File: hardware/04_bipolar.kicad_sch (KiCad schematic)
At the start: 22 parts, among them U4 TPS65131RGER

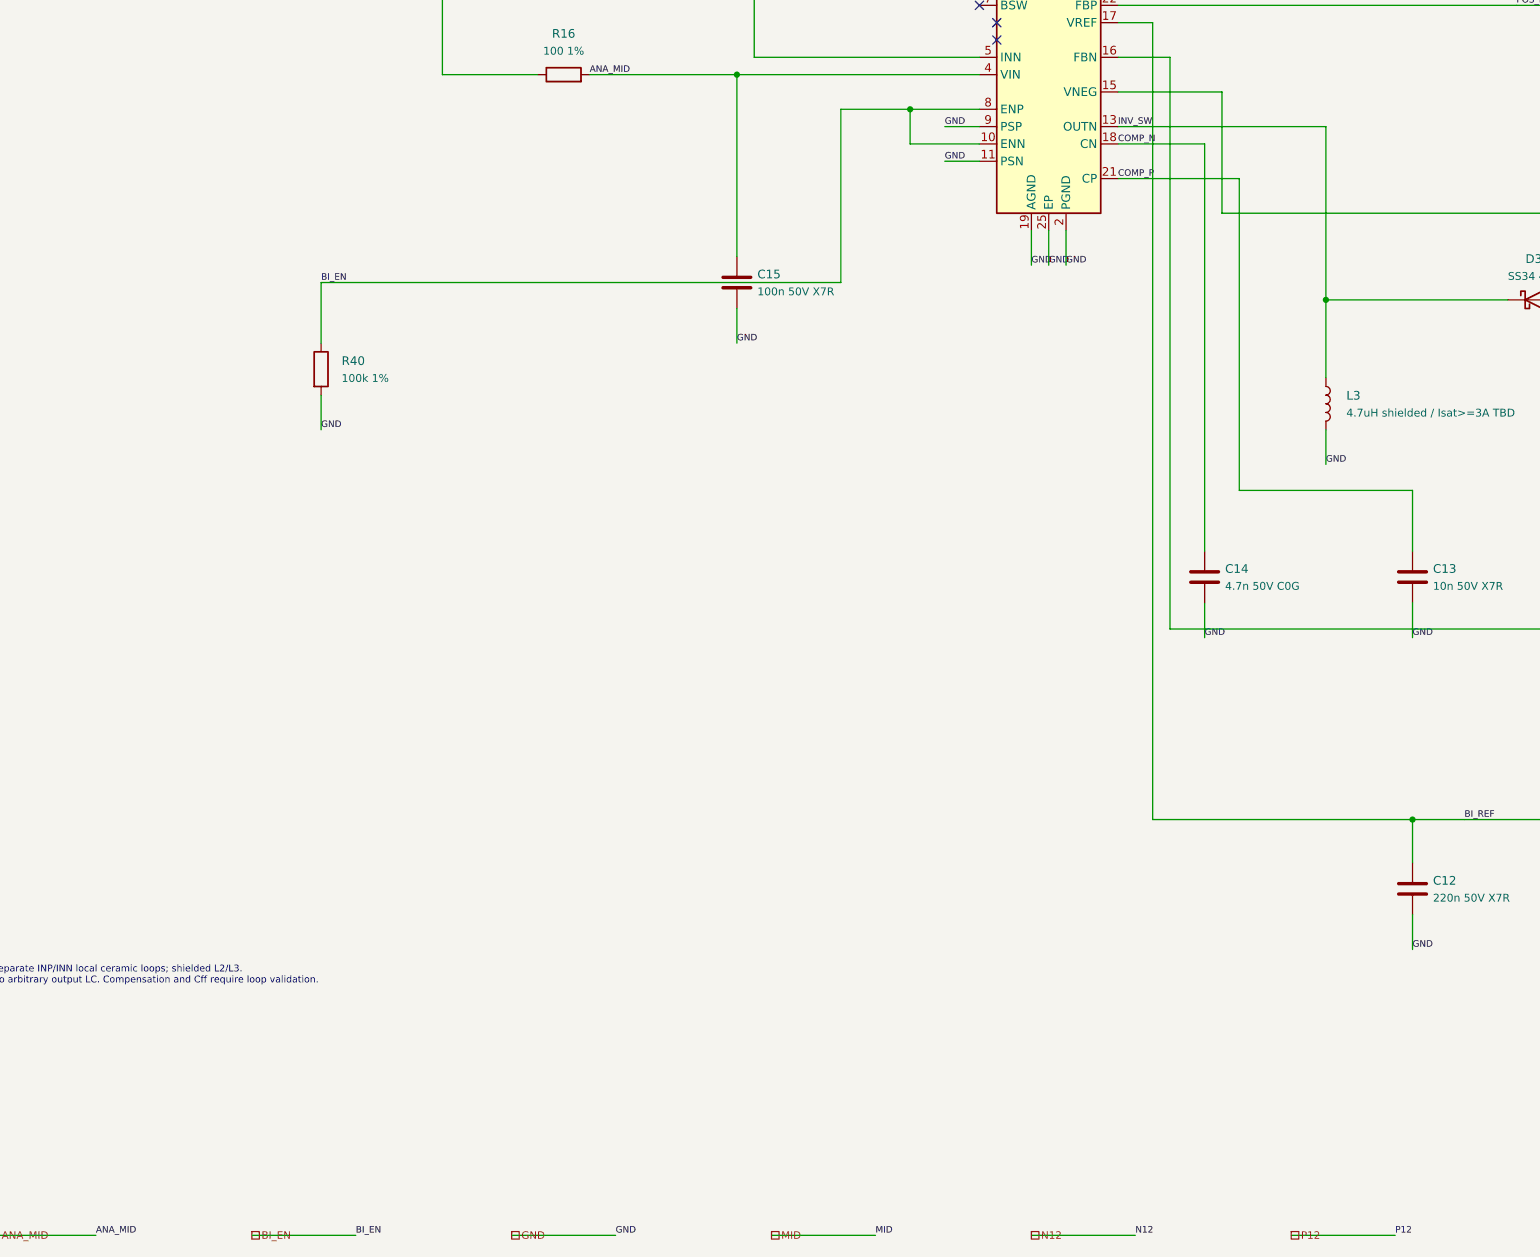
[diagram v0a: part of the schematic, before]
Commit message: Replace MCU diagnostics with optional rail-sense IDC and single 5 V power LED
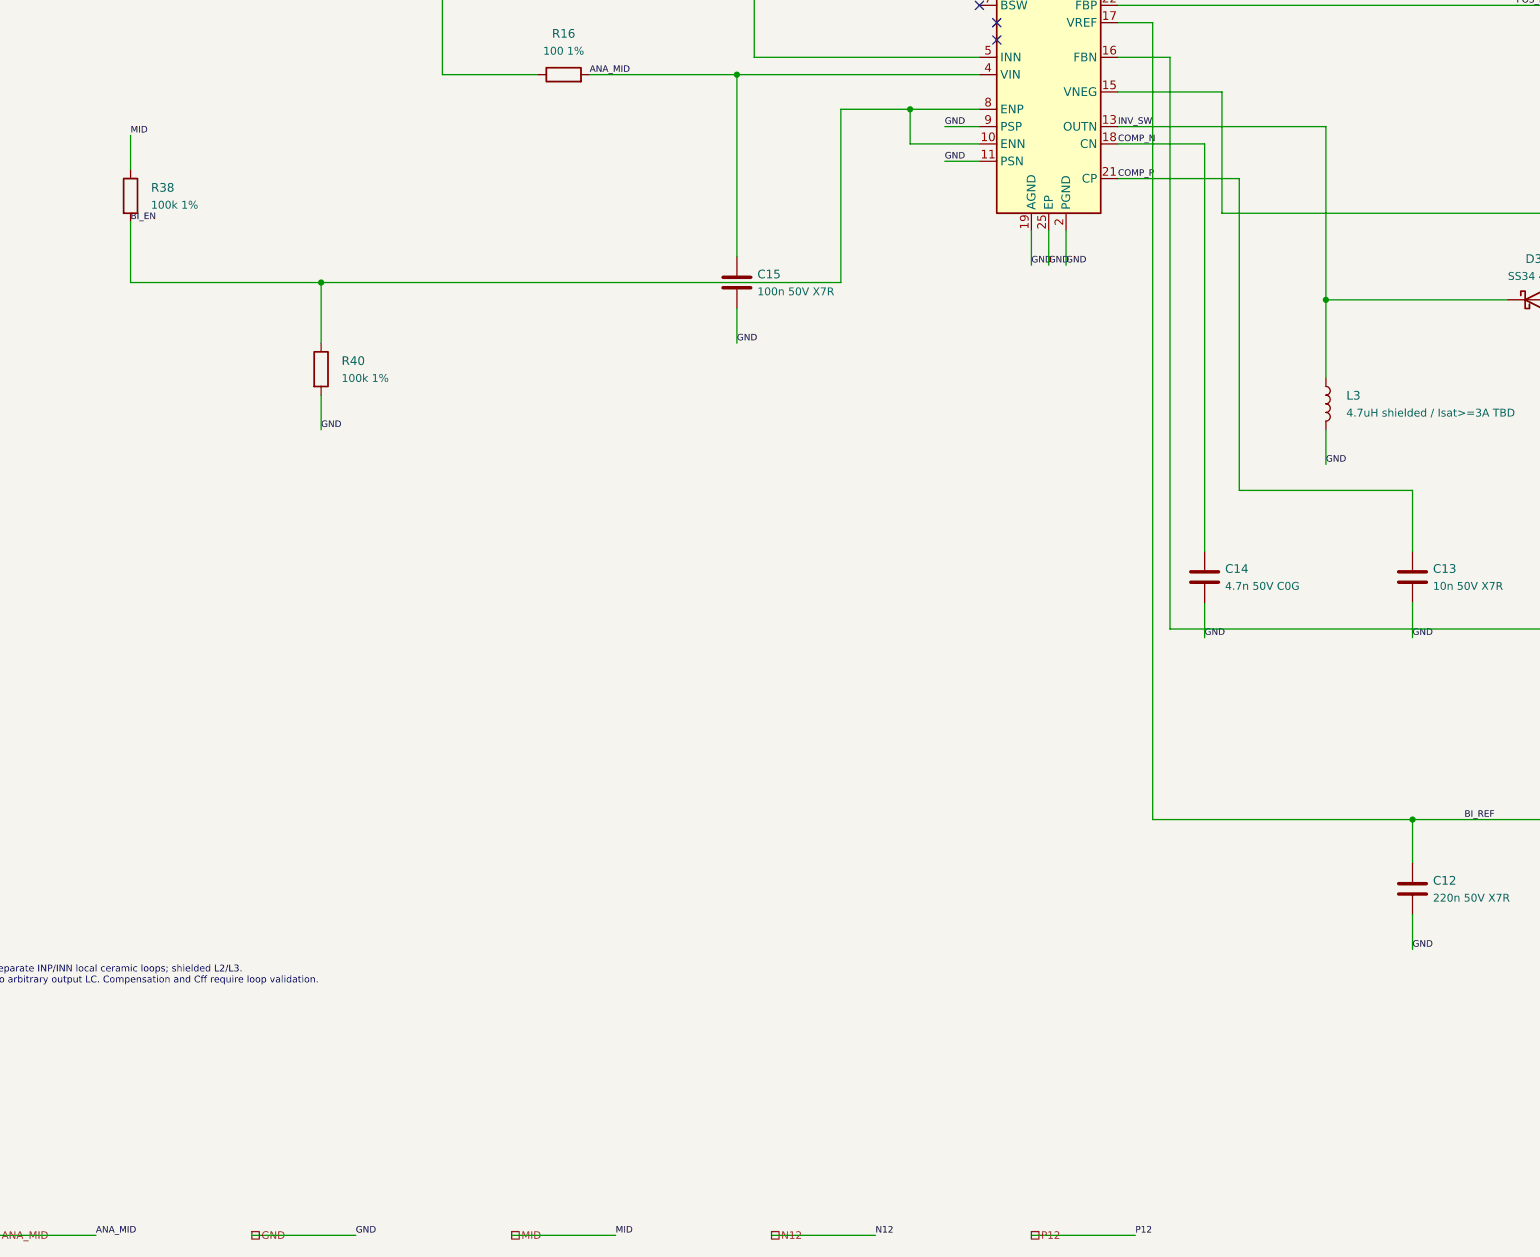
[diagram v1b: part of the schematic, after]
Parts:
- added R38: 100k 1%, BigModular:R_0603_1608Metric, symbol BigModular:Device_R
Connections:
- net BI_EN: now also R38.2
- net MID: now also R38.1

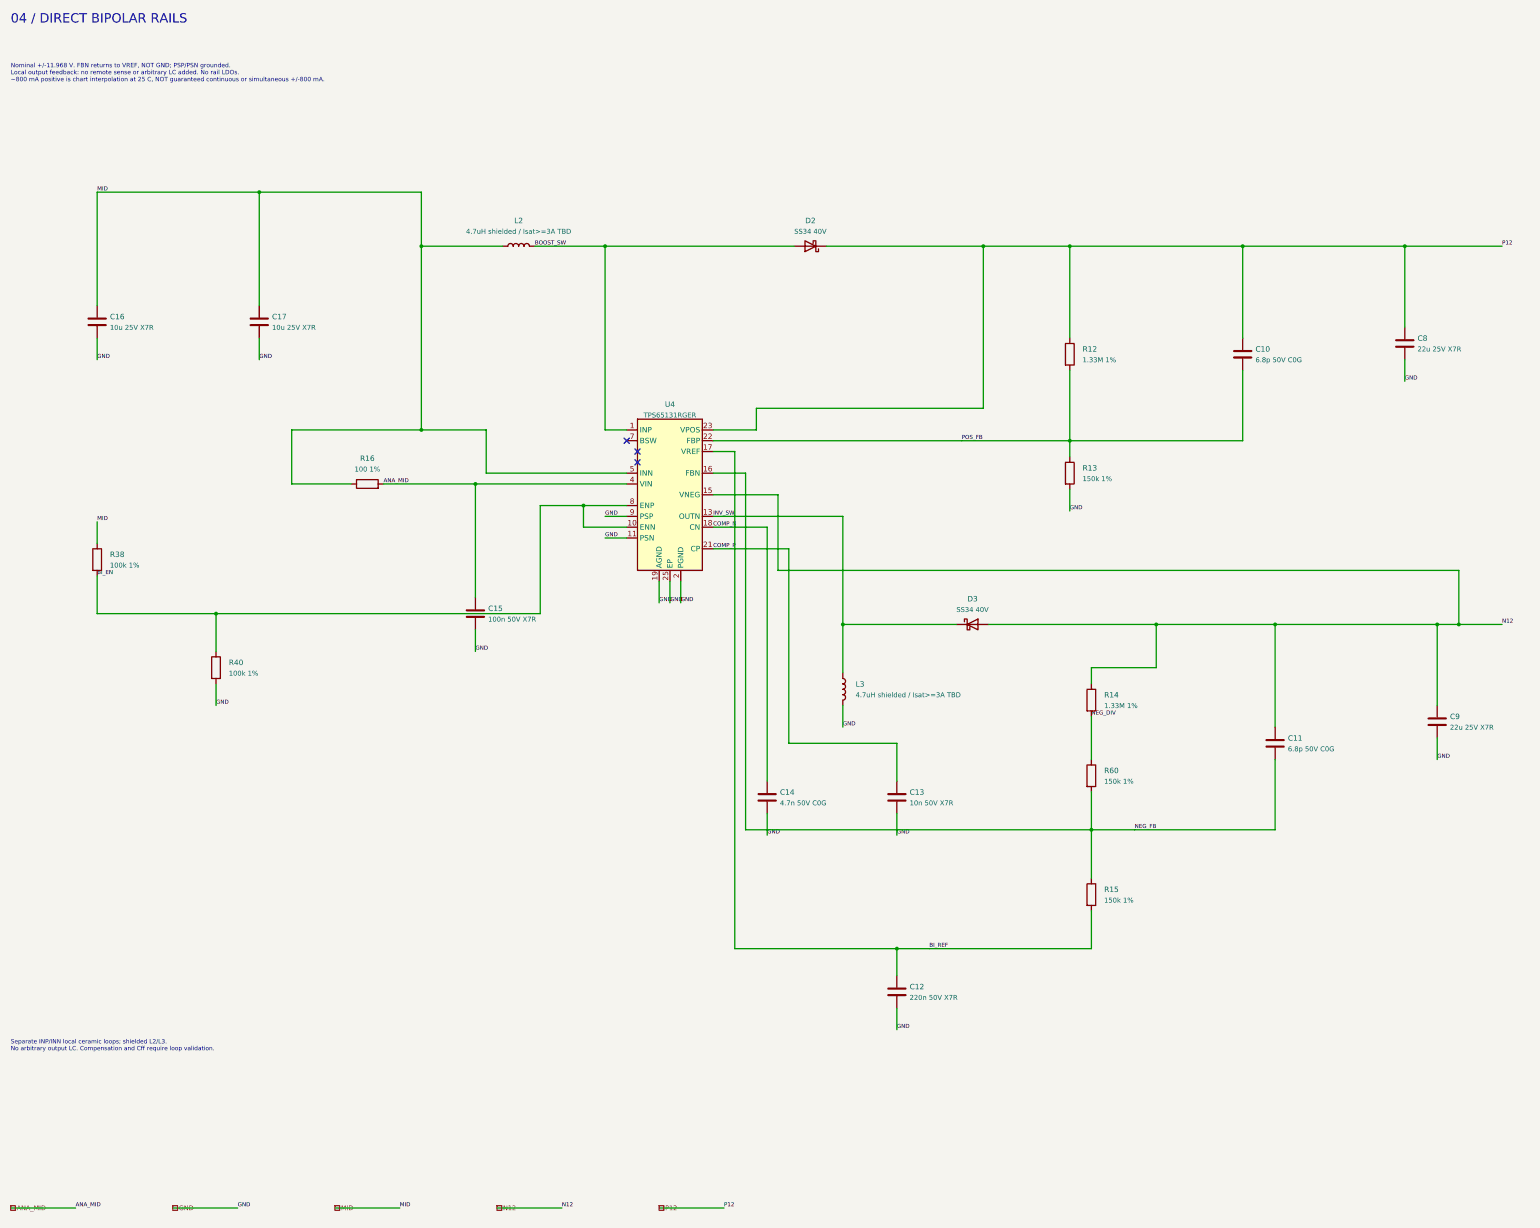
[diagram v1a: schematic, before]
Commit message: Clarify hierarchical ports and replace local label islands with visible schematic wiring
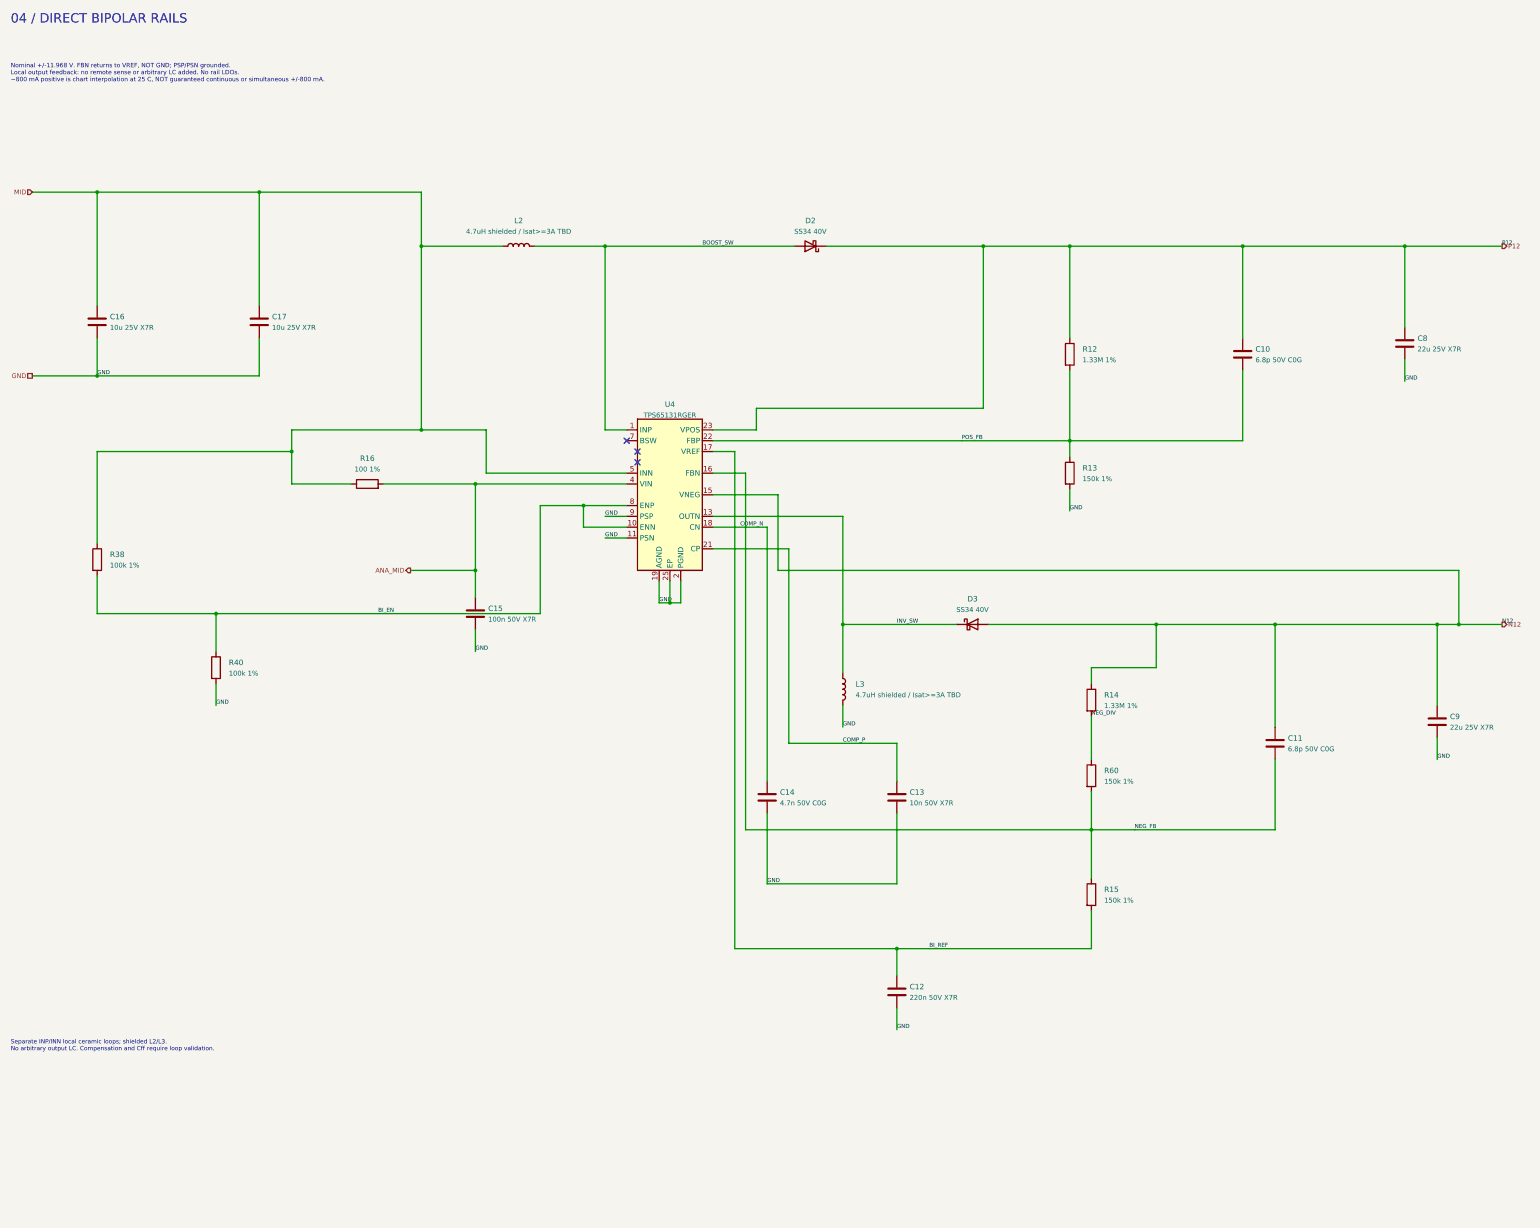
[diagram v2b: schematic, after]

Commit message: Simplify V1 power architecture, remove auxiliary sensing and obsolete documentation, enable autonomous protected start and reset button
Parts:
- D2, D3: NOTE Rectifier Vf/thermal/reverse transients and assembly polari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 -> Rectifier polarity, reverse transients and thermal behavior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
- L2, L3: value 4.7uH shielded / Isat>=3A TBD -> 4.7uH 20% shielded; footprint (none) -> BigModular:L_CENKER_CKCS6045; LCSC (none) -> C5291878; MPN (none) -> CKCS6045-4.7uH/M; NOTE Select exact shielded 4.7uH magnetic per TI table and verif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 -> CKCS6045-4.7uH/M; TI typical4.7uH, Isat4.97A, Irms3.30A. Ma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
- U4: footprint BigModular:Texas_RGE0024H_VQFN-24-1EP_4x4mm_P0.5mm_EP2.7x2.7mm -> BigModular:Texas_RGE0024B_VQFN-24-1EP_4x4mm_P0.5mm_EP2.45x2.45mm
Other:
- note added: "Nominal +/-11.968 V. FBN returns to VREF, NOT GND; PSP/PSN grounded. Local output feedback; no rail LDOs or extra output LC. L2/L3 4.7uH per TI typical application. Output current/ripple/thermal/transient limits need V1 validation; no simultaneous +/-800 mA rating."
- note removed: "Nominal +/-11.968 V. FBN returns to VREF, NOT GND; PSP/PSN grounded. Local output feedback: no remote sense or arbitrary LC added. No rail LDOs. ~800 mA positive is chart interpolation at 25 C, NOT guaranteed continuous or simultaneous +/-800 mA."
